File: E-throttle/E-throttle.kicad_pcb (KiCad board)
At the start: 2 copper layers, 100 x 100 mm, 69 parts, among them IC1 BTS441TG, J1 Conn_01x15_Socket, J2 Conn_01x15_Socket, J3 Conn_01x11, J4 Conn_01x11, J5 776087-1, J9 Micro_SD_Card, Q1 NMOS, SW1 SW_Push, U1 74HC123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

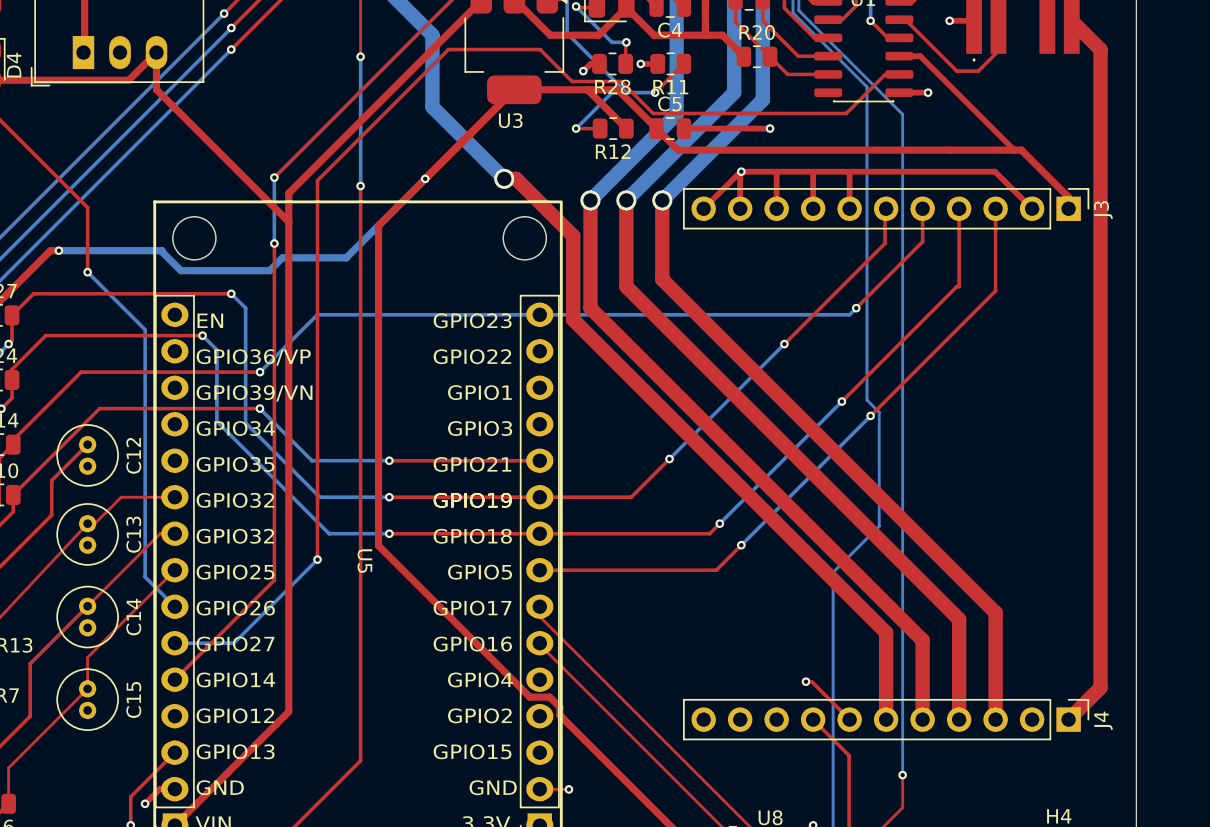
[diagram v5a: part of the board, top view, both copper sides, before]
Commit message: Changed Stepper motor driver headers to female headers
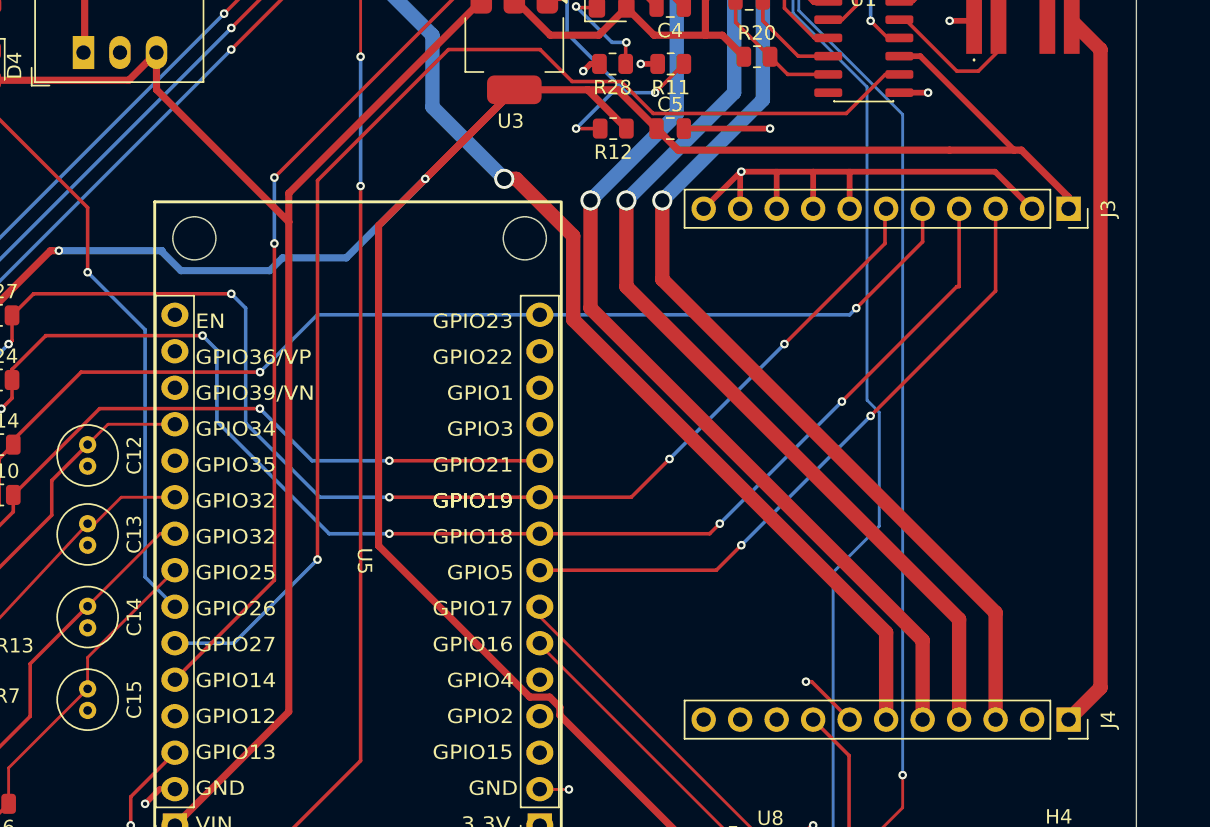
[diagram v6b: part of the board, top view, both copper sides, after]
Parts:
- J3, J4: footprint Connector_PinHeader_2.54mm:PinHeader_1x11_P2.54mm_Vertical -> Connector_PinSocket_2.54mm:PinSocket_1x11_P2.54mm_Vertical
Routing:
- net /APPS-SIG1-OUT: track 22.3 -> 29.0 mm
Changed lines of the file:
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@@
 	(net 79 "unconnected-(J2-Pin_4-Pad4)")
 	(net 80 "unconnected-(J2-Pin_13-Pad13)")
-	(footprint "Connector_PinHeader_2.54mm:PinHeader_1x11_P2.54mm_Vertical"
+	(footprint "Connector_PinSocket_2.54mm:PinSocket_1x11_P2.54mm_Vertical"
 		(layer "F.Cu")
 		(at 250 117.46 -90)
-		(descr "Through hole straight pin header, 1x11, 2.54mm pitch, single row")
-		(tags "Through hole pin header THT 1x11 2.54mm single row")
+		(descr "Through hole straight socket strip, 1x11, 2.54mm pitch, single row (from Kicad 4.0.7), script generated")
+		(tags "Through hole socket strip THT 1x11 2.54mm single row")
 		(property "Reference" "J4"
-			(at 0 -2.33 90)
+			(at 0 -2.77 270)
 			(layer "F.SilkS")
 			(effects
@@
 		)
 		(property "Value" "Conn_01x11"
-			(at 0 27.73 90)
+			(at 0 28.17 270)
 			(layer "F.Fab")
 			(effects
@@
 		(property "Datasheet" "~"
 			(at 0 0 270)
-			(unlocked yes)
 			(layer "F.Fab")
 			(hide yes)
@@
 		(property "Description" "Generic connector, single row, 01x11, script generated (kicad-library-utils/schlib/autogen/connector/)"
 			(at 0 0 270)
-			(unlocked yes)
 			(layer "F.Fab")
 			(hide yes)
@@
 		(attr through_hole)
 		(fp_line
-			(start -1.38 26.78)
-			(end 1.38 26.78)
+			(start -1.33 26.73)
+			(end 1.33 26.73)
 			(stroke
 				(width 0.12)
@@
 		)
 		(fp_line
-			(start -1.38 1.27)
-			(end -1.38 26.78)
+			(start -1.33 1.27)
+			(end -1.33 26.73)
 			(stroke
 				(width 0.12)
@@
 		)
 		(fp_line
-			(start -1.38 1.27)
-			(end 1.38 1.27)
+			(start -1.33 1.27)
+			(end 1.33 1.27)
 			(stroke
 				(width 0.12)
@@
 		)
 		(fp_line
-			(start 1.38 1.27)
-			(end 1.38 26.78)
+			(start 1.33 1.27)
+			(end 1.33 26.73)
 			(stroke
 				(width 0.12)
@@
 		)
 		(fp_line
-			(start -1.38 0)
-			(end -1.38 -1.38)
+			(start 0 -1.33)
+			(end 1.33 -1.33)
 			(stroke
 				(width 0.12)
@@
 		)
 		(fp_line
-			(start -1.38 -1.38)
-			(end 0 -1.38)
+			(start 1.33 -1.33)
+			(end 1.33 0)
 			(stroke
 				(width 0.12)
@@
 		)
 		(fp_line
-			(start -1.77 27.17)
-			(end 1.77 27.17)
+			(start -1.8 27.15)
+			(end -1.8 -1.8)
 			(stroke
 				(width 0.05)
@@
 		)
 		(fp_line
-			(start 1.77 27.17)
-			(end 1.77 -1.77)
+			(start 1.75 27.15)
+			(end -1.8 27.15)
 			(stroke
 				(width 0.05)
@@
 		)
 		(fp_line
-			(start -1.77 -1.77)
-			(end -1.77 27.17)
+			(start -1.8 -1.8)
+			(end 1.75 -1.8)
 			(stroke
 				(width 0.05)
@@
 		)
 		(fp_line
-			(start 1.77 -1.77)
-			(end -1.77 -1.77)
+			(start 1.75 -1.8)
+			(end 1.75 27.15)
 			(stroke
 				(width 0.05)
@@
 		(fp_line
 			(start -1.27 26.67)
-			(end -1.27 -0.635)
+			(end -1.27 -1.27)
 			(stroke
 				(width 0.1)
@@
 		)
 		(fp_line
-			(start -1.27 -0.635)
-			(end -0.635 -1.27)
+			(start 1.27 -0.635)
+			(end 1.27 26.67)
 			(stroke
 				(width 0.1)
@@
 		)
 		(fp_line
-			(start -0.635 -1.27)
-			(end 1.27 -1.27)
+			(start -1.27 -1.27)
+			(end 0.635 -1.27)
 			(stroke
 				(width 0.1)
@@
 		)
 		(fp_line
-			(start 1.27 -1.27)
-			(end 1.27 26.67)
+			(start 0.635 -1.27)
+			(end 1.27 -0.635)
 			(stroke
 				(width 0.1)
@@
 		)
 		(embedded_fonts no)
-		(model "${KICAD9_3DMODEL_DIR}/Connector_PinHeader_2.54mm.3dshapes/PinHeader_1x11_P2.54mm_Vertical.step"
+		(model "${KICAD9_3DMODEL_DIR}/Connector_PinSocket_2.54mm.3dshapes/PinSocket_1x11_P2.54mm_Vertical.step"
 			(offset
 				(xyz 0 0 0)
@@
 		)
 	)
-	(footprint "Connector_PinHeader_2.54mm:PinHeader_1x11_P2.54mm_Vertical"
+	(footprint "Connector_PinSocket_2.54mm:PinSocket_1x11_P2.54mm_Vertical"
 		(locked yes)
 		(layer "F.Cu")
 		(at 250 81.9 -90)
-		(descr "Through hole straight pin header, 1x11, 2.54mm pitch, single row")
-		(tags "Through hole pin header THT 1x11 2.54mm single row")
+		(descr "Through hole straight socket strip, 1x11, 2.54mm pitch, single row (from Kicad 4.0.7), script generated")
+		(tags "Through hole socket strip THT 1x11 2.54mm single row")
 		(property "Reference" "J3"
-			(at 0 -2.33 90)
+			(at 0 -2.77 270)
 			(layer "F.SilkS")
 			(effects
@@
 		)
 		(property "Value" "Conn_01x11"
-			(at 0 25.952 90)
+			(at 0 28.17 270)
 			(layer "F.Fab")
 			(effects
@@
 		(property "Datasheet" "~"
 			(at 0 0 270)
-			(unlocked yes)
 			(layer "F.Fab")
 			(hide yes)
@@
 		(property "Description" "Generic connector, single row, 01x11, script generated (kicad-library-utils/schlib/autogen/connector/)"
 			(at 0 0 270)
-			(unlocked yes)
 			(layer "F.Fab")
 			(hide yes)
@@
 		(attr through_hole)
 		(fp_line
-			(start -1.38 26.78)
-			(end 1.38 26.78)
+			(start -1.33 26.73)
+			(end 1.33 26.73)
 			(stroke
 				(width 0.12)
@@
 		)
 		(fp_line
-			(start -1.38 1.27)
-			(end -1.38 26.78)
+			(start -1.33 1.27)
+			(end -1.33 26.73)
 			(stroke
 				(width 0.12)
@@
 		)
 		(fp_line
-			(start -1.38 1.27)
-			(end 1.38 1.27)
+			(start -1.33 1.27)
+			(end 1.33 1.27)
 			(stroke
 				(width 0.12)
@@
 		)
 		(fp_line
-			(start 1.38 1.27)
-			(end 1.38 26.78)
+			(start 1.33 1.27)
+			(end 1.33 26.73)
 			(stroke
 				(width 0.12)
@@
 		)
 		(fp_line
-			(start -1.38 0)
-			(end -1.38 -1.38)
+			(start 0 -1.33)
+			(end 1.33 -1.33)
 			(stroke
 				(width 0.12)
@@
 		)
 		(fp_line
-			(start -1.38 -1.38)
-			(end 0 -1.38)
+			(start 1.33 -1.33)
+			(end 1.33 0)
 			(stroke
 				(width 0.12)
@@
 		)
 		(fp_line
-			(start -1.77 27.17)
-			(end 1.77 27.17)
+			(start -1.8 27.15)
+			(end -1.8 -1.8)
 			(stroke
 				(width 0.05)
@@
 		)
 		(fp_line
-			(start 1.77 27.17)
-			(end 1.77 -1.77)
+			(start 1.75 27.15)
+			(end -1.8 27.15)
 			(stroke
 				(width 0.05)
@@
 		)
 		(fp_line
-			(start -1.77 -1.77)
-			(end -1.77 27.17)
+			(start -1.8 -1.8)
+			(end 1.75 -1.8)
 			(stroke
 				(width 0.05)
@@
 		)
 		(fp_line
-			(start 1.77 -1.77)
-			(end -1.77 -1.77)
+			(start 1.75 -1.8)
+			(end 1.75 27.15)
 			(stroke
 				(width 0.05)
@@
 		(fp_line
 			(start -1.27 26.67)
-			(end -1.27 -0.635)
+			(end -1.27 -1.27)
 			(stroke
 				(width 0.1)
@@
 		)
 		(fp_line
-			(start -1.27 -0.635)
-			(end -0.635 -1.27)
+			(start 1.27 -0.635)
+			(end 1.27 26.67)
 			(stroke
 				(width 0.1)
@@
 		)
 		(fp_line
-			(start -0.635 -1.27)
-			(end 1.27 -1.27)
+			(start -1.27 -1.27)
+			(end 0.635 -1.27)
 			(stroke
 				(width 0.1)
@@
 		)
 		(fp_line
-			(start 1.27 -1.27)
-			(end 1.27 26.67)
+			(start 0.635 -1.27)
+			(end 1.27 -0.635)
 			(stroke
 				(width 0.1)
@@
 		)
 		(embedded_fonts no)
-		(model "${KICAD9_3DMODEL_DIR}/Connector_PinHeader_2.54mm.3dshapes/PinHeader_1x11_P2.54mm_Vertical.step"
+		(model "${KICAD9_3DMODEL_DIR}/Connector_PinSocket_2.54mm.3dshapes/PinSocket_1x11_P2.54mm_Vertical.step"
 			(offset
 				(xyz 0 0 0)
@@
 	)
 	(segment
-		(start 216.52 73.62)
-		(end 218.62 73.62)
-		(width 0.5)
-		(layer "F.Cu")
-		(net 5)
-	)
-	(segment
 		(start 162.72 73.87)
 		(end 162.72 81.495)
@@
 	)
 	(segment
+		(start 218.62 73.62)
+		(end 216.52 73.62)
+		(width 0.5)
+		(layer "F.Cu")
+		(net 5)
+	)
+	(segment
 		(start 160.72 66.82)
 		(end 160.72 62.82)
@@
 	)
 	(segment
+		(start 187.79246 96.899813)
+		(end 183.140187 96.899813)
+		(width 0.2)
+		(layer "F.Cu")
+		(net 50)
+	)
+	(segment
 		(start 170.1325 112.32)
 		(end 179.22 103.2325)
@@
 		(layer "F.Cu")
 		(net 50)
+	)
+	(segment
+		(start 183.140187 96.899813)
+		(end 181.72 98.32)
+		(width 0.2)
+		(layer "F.Cu")
+		(net 50)

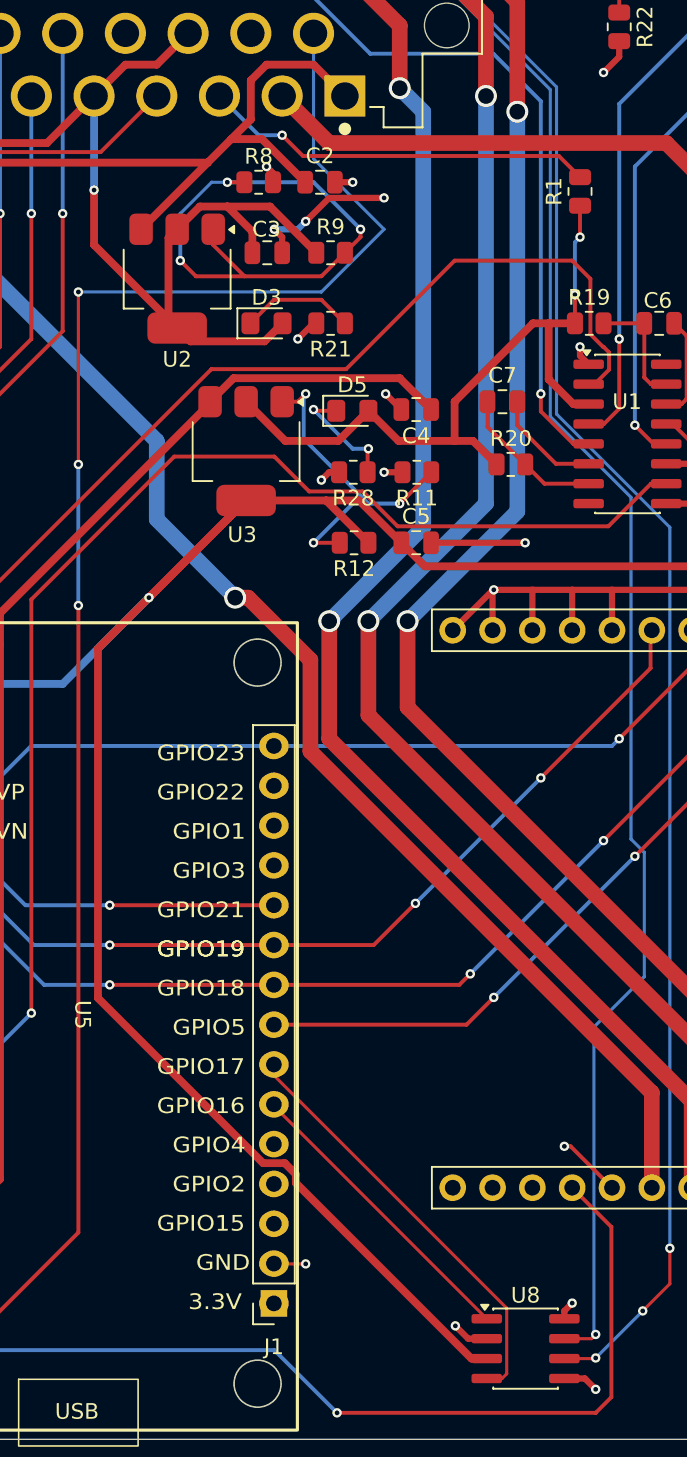
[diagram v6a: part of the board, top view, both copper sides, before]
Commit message: Deleted IDLE Control circuit
Fully disconnected IDLE control pin from loom
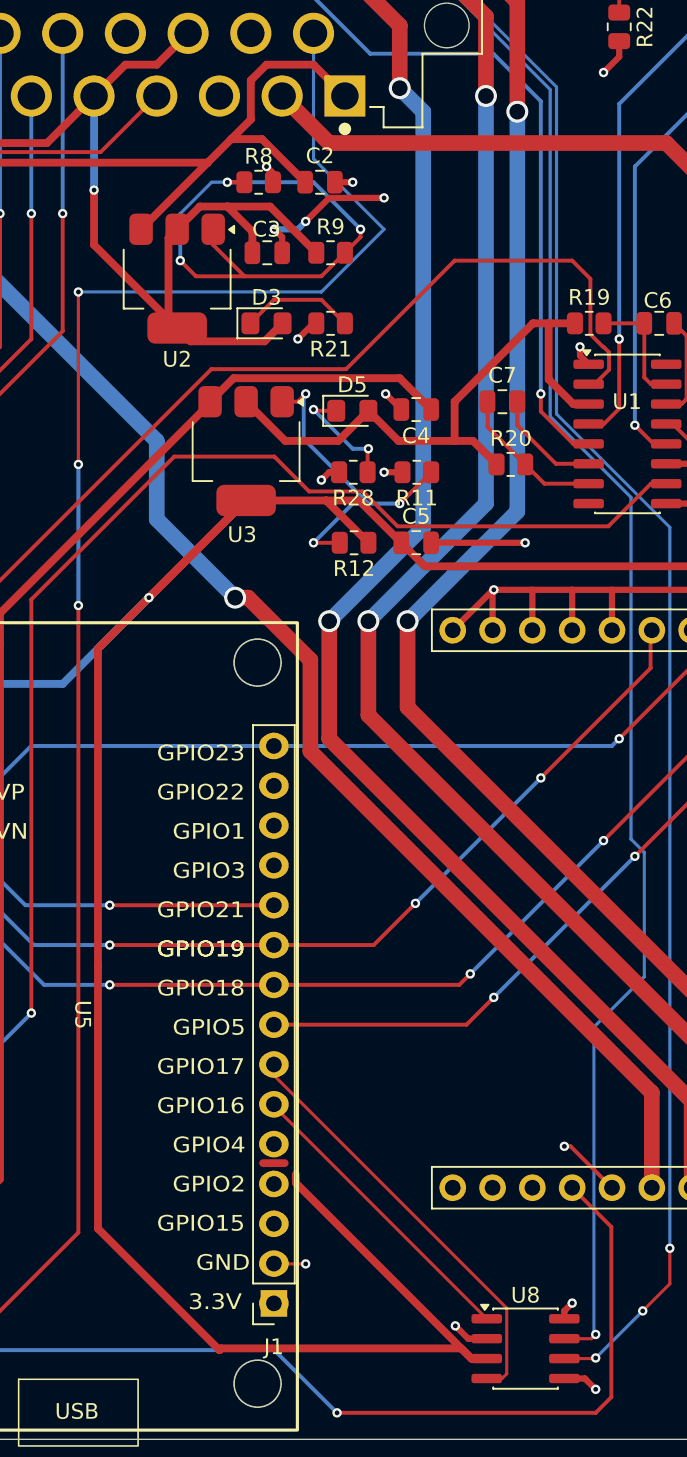
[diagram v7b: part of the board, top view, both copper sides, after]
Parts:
- removed R1: 100k, Resistor_SMD:R_0805_2012Metric
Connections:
- J1 pad 5: /IDLE -> unconnected-(J1-Pin_5-Pad5)
- U5 pad 20: /IDLE -> unconnected-(U5-D4-Pad20)
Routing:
- net /IDLE: track 25.1 -> 0.00 mm, vias 1 -> 0
- net +3V3: track 310.1 -> 328.6 mm, vias 4 -> 2
